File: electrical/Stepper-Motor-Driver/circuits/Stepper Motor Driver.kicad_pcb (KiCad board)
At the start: 4 copper layers, 100 x 100 mm, 172 parts, among them J1 Screw_Terminal_01x03, J10 Conn_01x01_Socket, J11 Conn_01x01_Socket, J12 Conn_01x01_Socket, J13 Conn_01x01_Socket, J14 Conn_01x01_Socket, J15 Conn_01x01_Socket, J16 Conn_01x01_Socket, J17 Conn_01x01_Socket, J18 Conn_01x01_Socket, J19 Conn_01x01_Socket, J2 Screw_Terminal_01x04, J20 Conn_01x01_Socket, J21 Conn_01x01_Socket, J22 Conn_01x01_Socket, J23 Conn_01x01_Socket, J8 Conn_01x01_Socket, J9 Conn_01x01_Socket, Q1 IRF530NPBF, Q2 IRF530NPBF, Q3 IRF530NPBF, Q4 IRF530NPBF, Q5 IRF530NPBF, Q6 IRF530NPBF, Q7 IRF530NPBF, Q8 IRF530NPBF, U10 LM1117-Q1, U11 TPS54202DDC, U12 REF2033, U2 UCC27710D, U3 UCC27710D, U4 UCC27710D, U5 UCC27710D, U6 INA240A2PW, U7 ADS7042xDCU, U8 INA240A2PW, U9 ADS7042xDCU

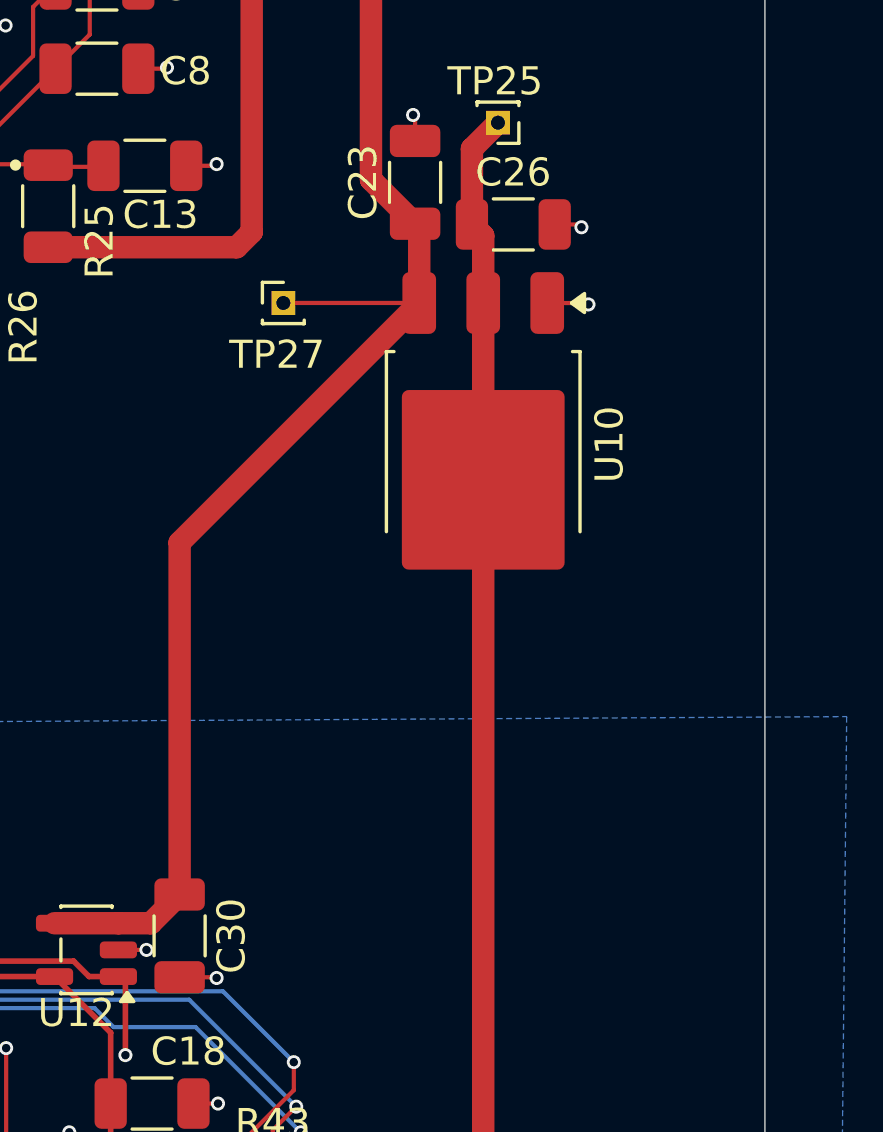
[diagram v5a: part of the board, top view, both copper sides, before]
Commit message: Adding thermal relief pad under LDO
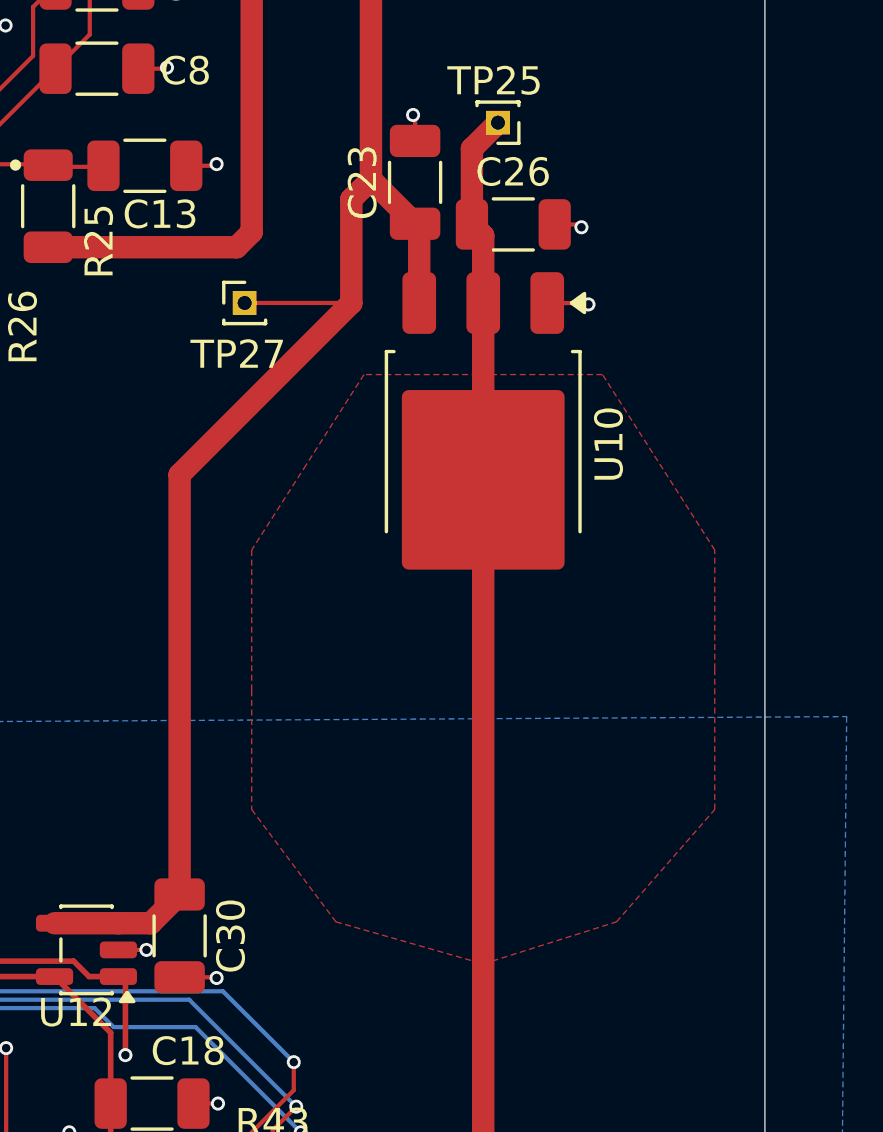
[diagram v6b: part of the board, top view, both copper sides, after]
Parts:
- moved TP27 1.38 mm to (187.5, 77.2)
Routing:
- net +5V: track 67.4 -> 70.1 mm
- added copper zone on F.Cu, net +3.3V
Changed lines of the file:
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@@
 	(footprint "Connector_PinHeader_1.00mm:PinHeader_1x01_P1.00mm_Vertical"
 		(layer "F.Cu")
-		(at 188.876958 77.198198)
+		(at 187.5 77.198198)
 		(descr "Through hole straight pin header, 1x01, 1.00mm pitch, single row")
 		(tags "Through hole pin header THT 1x01 1.00mm single row")
@@
 			(layers "F.Paste")
 			(roundrect_rratio 0.090909)
+			(zone_connect 2)
 		)
 		(pad "" smd roundrect
@@
 			(layers "F.Paste")
 			(roundrect_rratio 0.090909)
+			(zone_connect 2)
 		)
 		(pad "" smd roundrect
@@
 			(layers "F.Paste")
 			(roundrect_rratio 0.090909)
+			(zone_connect 2)
 		)
 		(pad "" smd roundrect
@@
 			(layers "F.Paste")
 			(roundrect_rratio 0.090909)
+			(zone_connect 2)
 		)
 		(pad "1" smd roundrect
@@
 	)
 	(segment
-		(start 188.876958 77.198198)
-		(end 193.718198 77.198198)
-		(width 0.15)
+		(start 185.18125 98.275)
+		(end 185.18125 83.31875)
+		(width 0.8)
 		(layer "F.Cu")
 		(net "+5V")
@@
 	)
 	(segment
+		(start 185.18125 83.31875)
+		(end 191.3 77.2)
+		(width 0.8)
+		(layer "F.Cu")
+		(net "+5V")
+	)
+	(segment
 		(start 183 99.3)
 		(end 184.15625 99.3)
@@
 	)
 	(segment
-		(start 185.18125 85.73875)
-		(end 193.72 77.2)
+		(start 191.3 77.2)
+		(end 191.3 73.5025)
 		(width 0.8)
 		(layer "F.Cu")
@@
 	)
 	(segment
+		(start 191.298198 77.198198)
+		(end 187.5 77.198198)
+		(width 0.15)
+		(layer "F.Cu")
+		(net "+5V")
+	)
+	(segment
 		(start 192 65.525)
 		(end 195.025 62.5)
@@
 	)
 	(segment
-		(start 195.1 57)
-		(end 195.1 62.425)
+		(start 191.3 73.5025)
+		(end 192 72.8025)
 		(width 0.8)
 		(layer "F.Cu")
@@
 	)
 	(segment
-		(start 185.18125 98.275)
-		(end 185.18125 85.73875)
+		(start 195.1 57)
+		(end 195.1 62.425)
 		(width 0.8)
 		(layer "F.Cu")
@@
 	)
 	(zone
+		(net "+3.3V")
+		(layer "F.Cu")
+		(name "Thermal Relief")
+		(hatch edge 0.5)
+		(priority 2)
+		(connect_pads yes
+			(clearance 0.5)
+		)
+		(min_thickness 0.25)
+		(fill yes
+			(thermal_gap 0.5)
+			(thermal_bridge_width 0.5)
+			(island_removal_mode 0)
+		)
+		(polygon
+			(pts
+				(xy 191.75 79.75) (xy 189.69 82.97) (xy 187.75 86) (xy 187.75 91) (xy 187.75 95.25) (xy 190.75 99.25)
+				(xy 196 100.75) (xy 200.75 99.25) (xy 204.25 95.25) (xy 204.25 90.25) (xy 204.25 86) (xy 200.25 79.75)
+			)
+		)
+	)
+	(zone

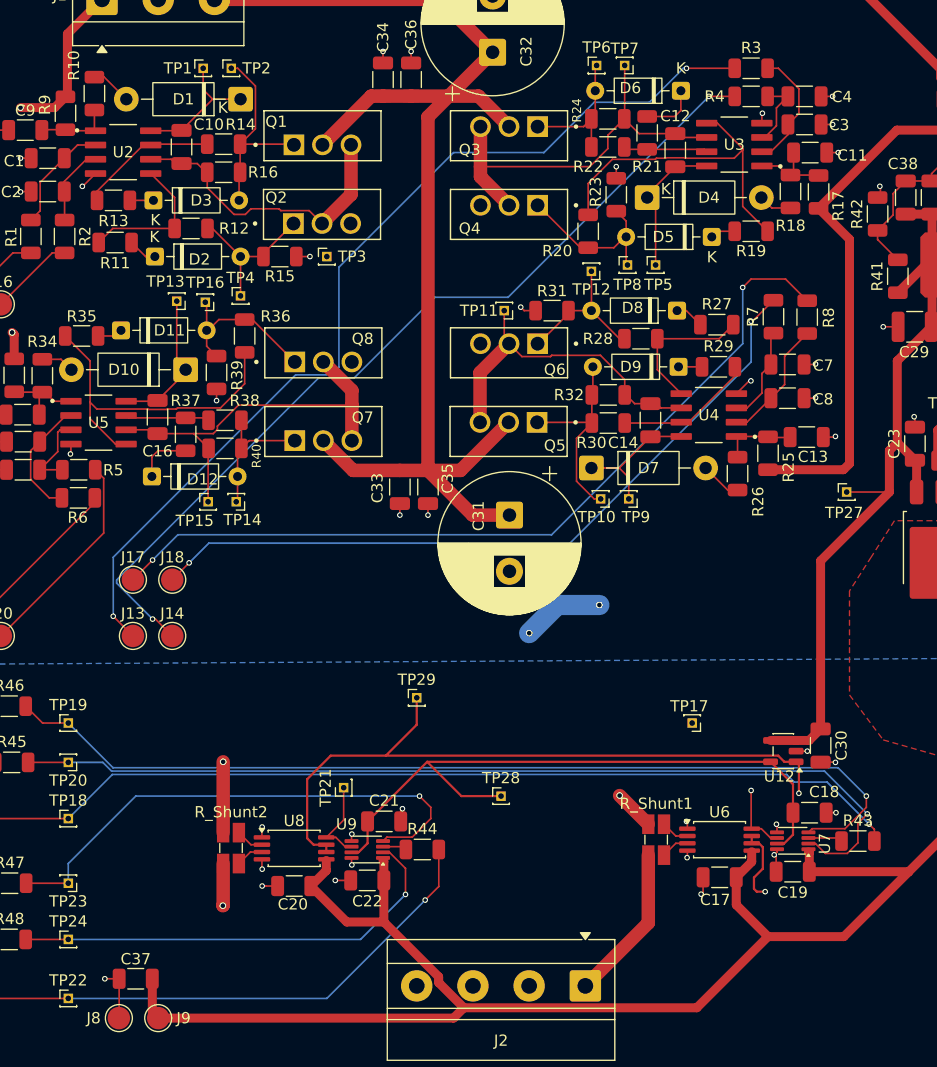
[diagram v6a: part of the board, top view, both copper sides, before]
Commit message: Rerouting power on L4
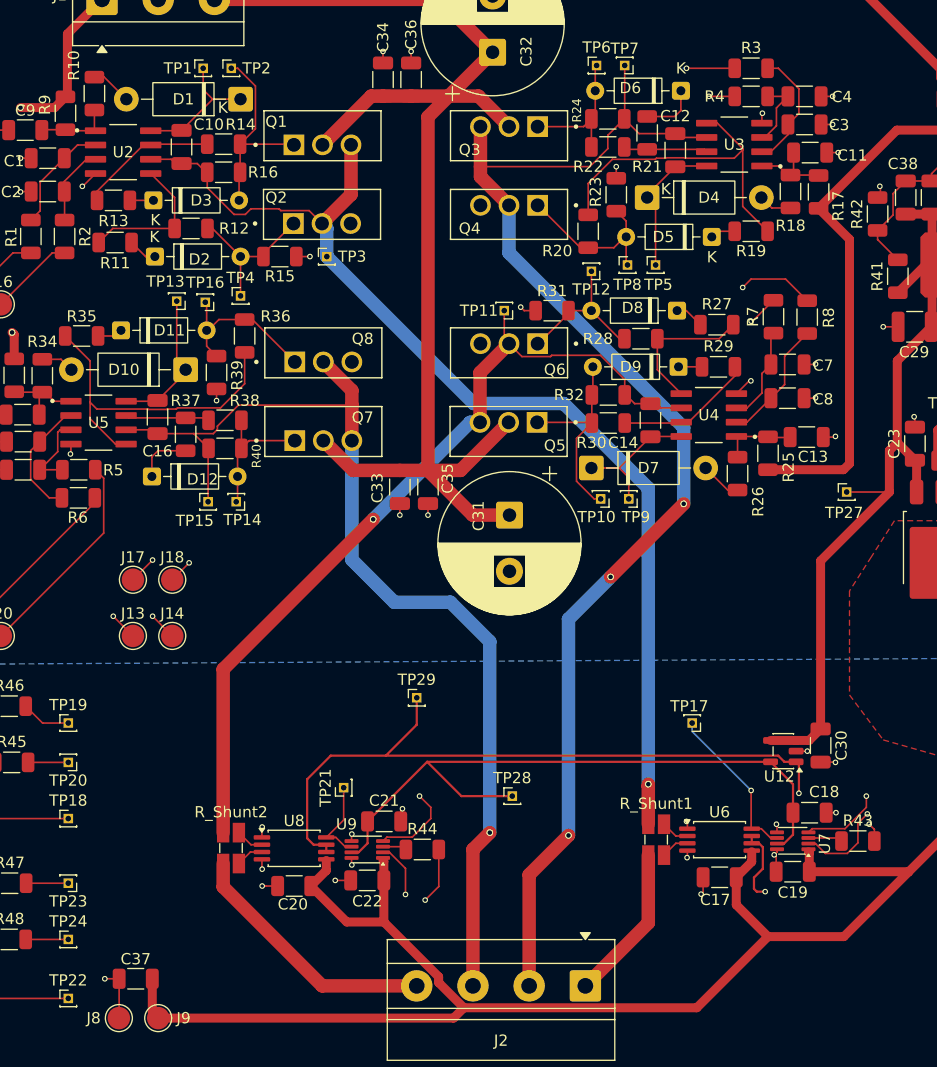
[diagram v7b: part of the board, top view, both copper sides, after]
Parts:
- moved TP28 1.00 mm to (157.8, 104.2)
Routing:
- net /H-Bridge Controller B/BR2: track 114.9 -> 93.3 mm, vias 0 -> 1
- net /Current Sensor A/IN+: track 101.6 -> 97.6 mm
- net /LI2A: track 80.0 -> 78.7 mm
- net /Current Sensor B/IN-: track 24.0 -> 22.9 mm, vias 1 -> 0
- net +3.3V-REF: track 58.6 -> 59.6 mm
- net /Current Sensor B/IN+: track 75.2 -> 75.7 mm
- net /H-Bridge Controller A/BR2: track 118.1 -> 117.7 mm, vias 2 -> 3

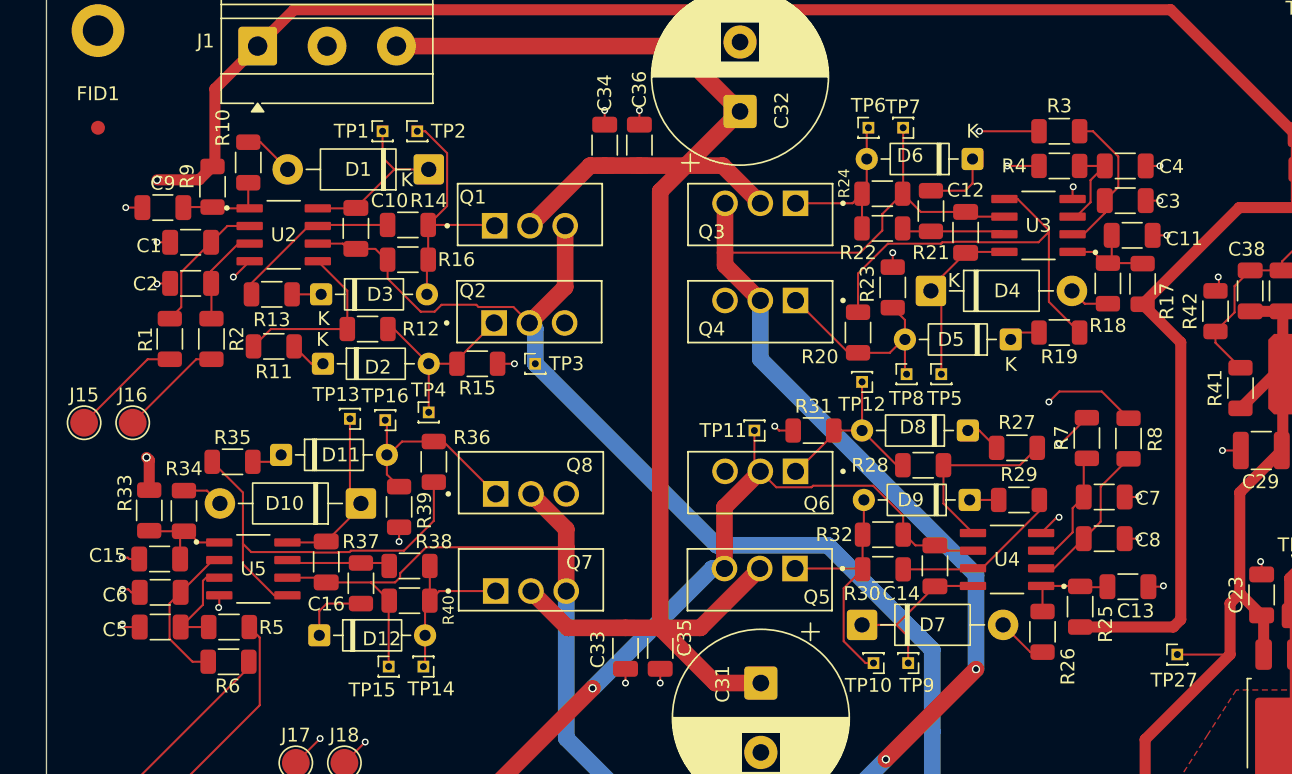
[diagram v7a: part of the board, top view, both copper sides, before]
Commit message: Optimized capacitor placement
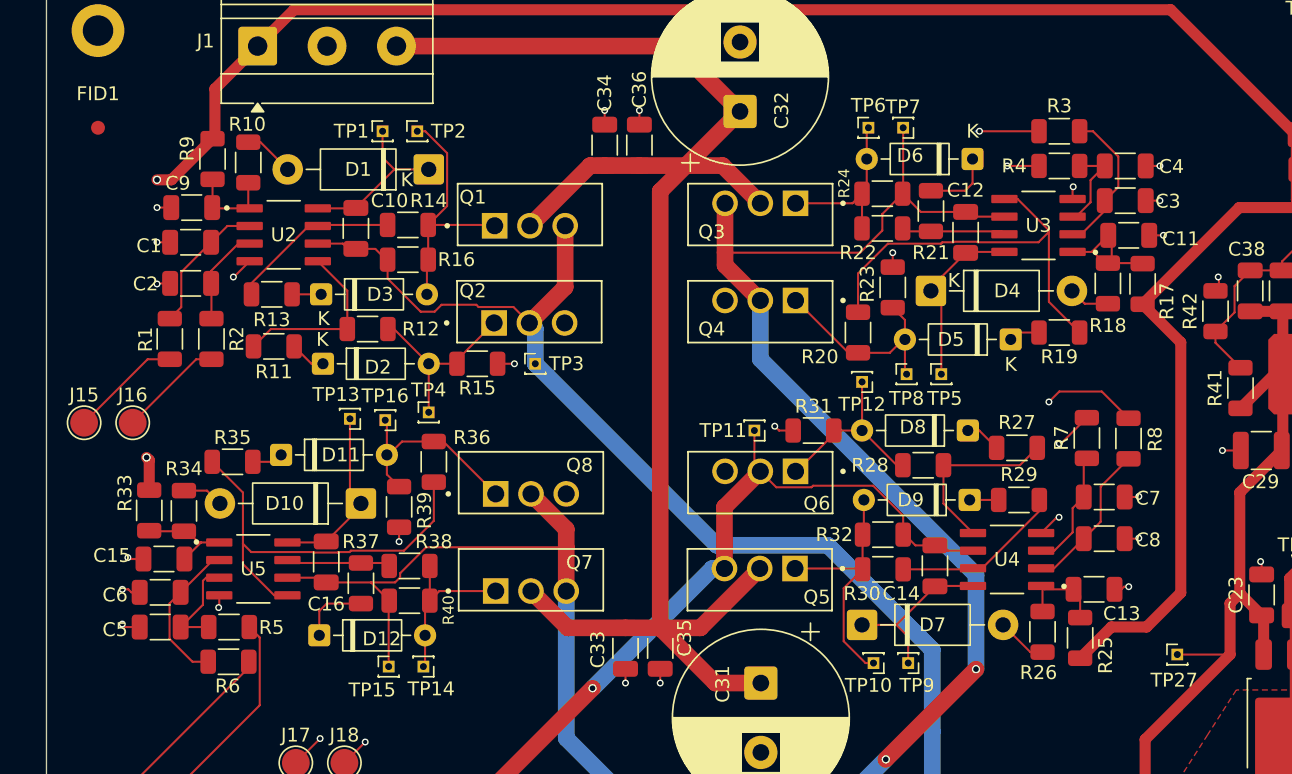
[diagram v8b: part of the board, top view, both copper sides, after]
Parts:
- moved C13 2.45 mm to (181.5, 72.5)
- moved R25 2.25 mm to (180.5, 76.0)
- moved C9 2.08 mm to (116.5, 45.0)
- moved R9 2.00 mm to (118.0, 41.5)
- moved C15 0.31 mm to (114.5, 70.3)
- moved C11 0.25 mm to (184.0, 47.0)
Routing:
- net Net-(U3-VDD): track 7.51 -> 9.30 mm
- net +12V: track 168.7 -> 167.3 mm
